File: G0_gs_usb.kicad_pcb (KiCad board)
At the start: 2 copper layers, 25.9 x 53.3 mm, 54 parts, among them J1 USB_C_Receptacle_USB2.0, J2 CAN1, J3 CAN2, J4 Conn_01x03_Pin, U1 STM32G0B1CBTx, U2 TJA1042T-3, U3 TJA1042T-3, U4 XC6206PxxxMR

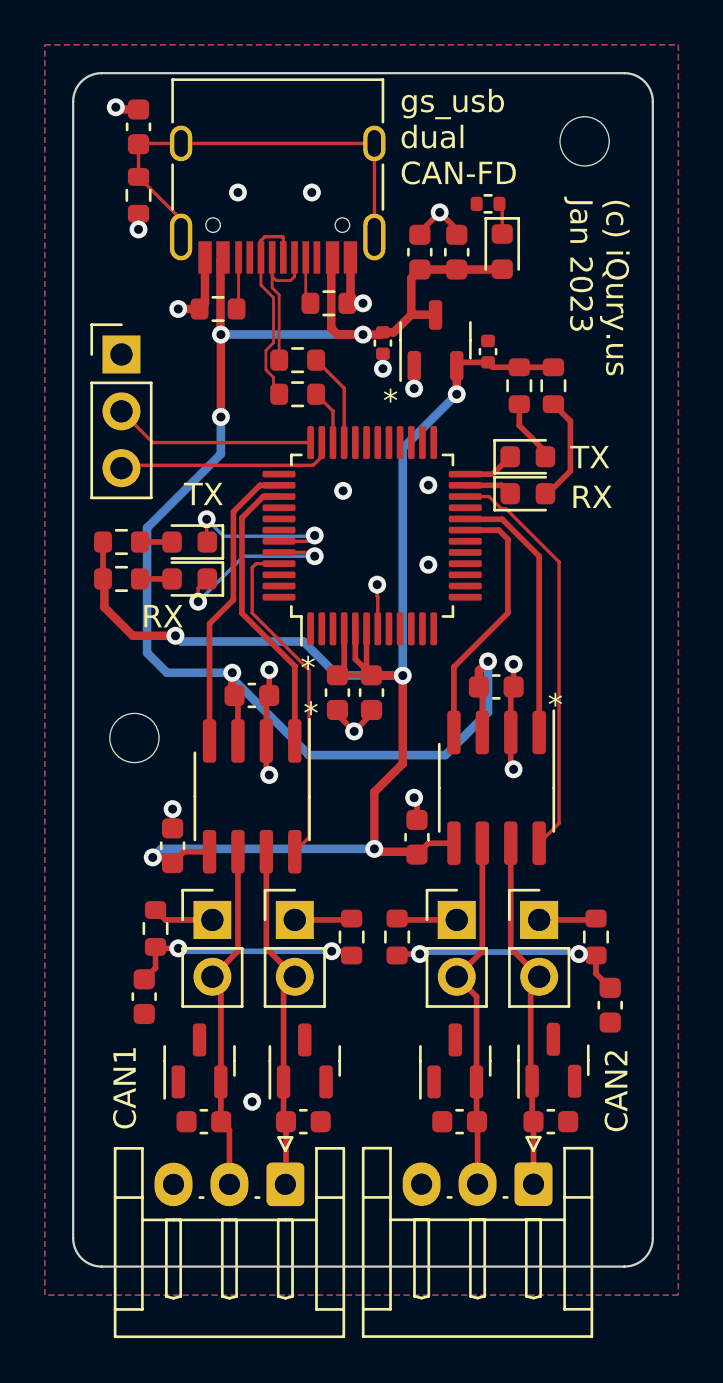
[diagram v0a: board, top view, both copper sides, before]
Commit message: Update footprints on R and C to 0402. Added 5V protection. Routed CAN RX/TX as diff pairs.
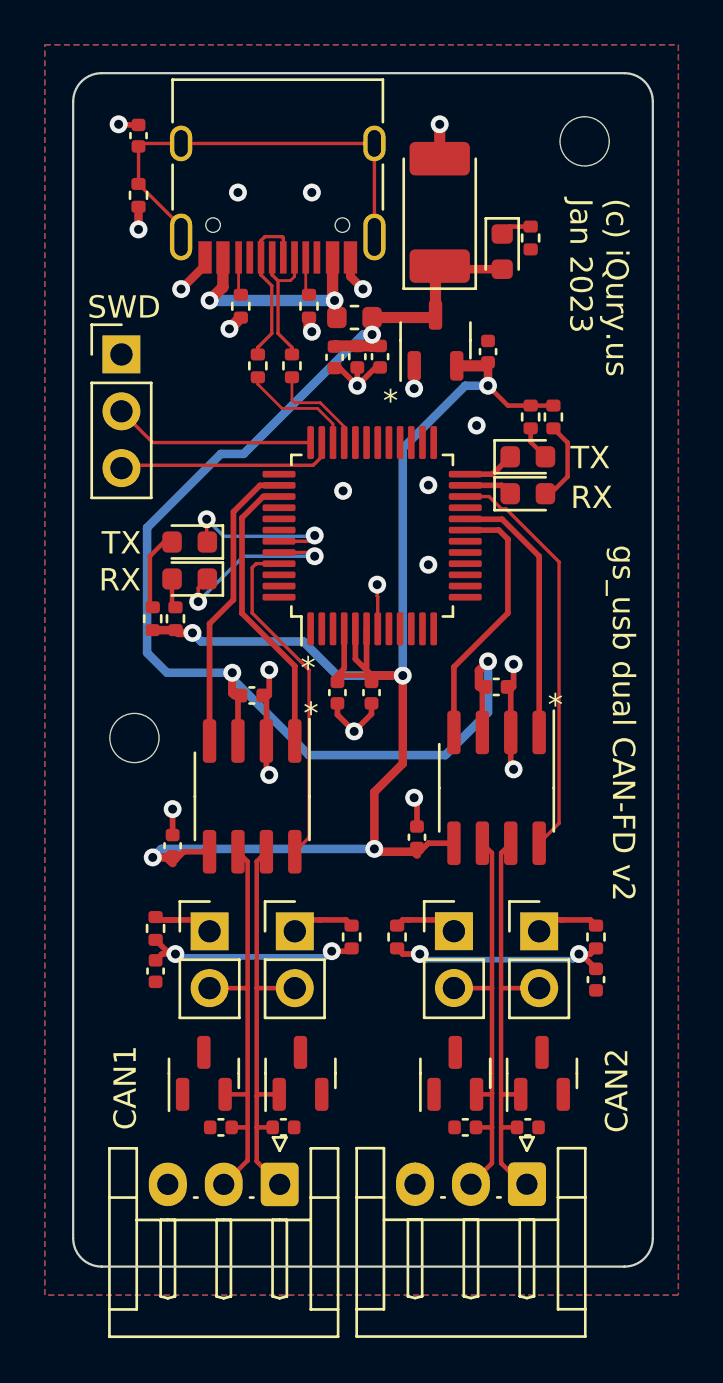
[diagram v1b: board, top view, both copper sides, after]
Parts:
- added D1: 5.3V, Diode_SMD:D_MELF, F.Cu at (68.5, 69.7)
- added F1: 500mA, Fuse:Fuse_0603_1608Metric, F.Cu at (64.6, 74.4)
- C1, C10, C11, C12, C13, C14, C15, C2, C3, C4, C5, C6, C7, C8, C9: footprint Capacitor_SMD:C_0603_1608Metric -> Capacitor_SMD:C_0402_1005Metric
- R1, R10, R11, R12, R13, R2, R3, R4, R5, R6, R7, R8, R9: footprint Resistor_SMD:R_0603_1608Metric -> Resistor_SMD:R_0402_1005Metric
- moved C13 6.45 mm to (64.8, 76.2), turned to 90 degrees
- moved C12 5.00 mm to (65.8, 76.2), turned to 90 degrees
- moved R11 3.70 mm to (55.6, 87.9), turned to 90 degrees
- moved R13 3.00 mm to (56.6, 87.9), turned to 90 degrees
- moved R14 2.44 mm to (72.5, 70.9), turned to -90 degrees
- moved C16 2.25 mm to (63.8, 76.2)
- moved R4 2.18 mm to (60.3, 76.6), turned to -90 degrees
- moved R12 1.48 mm to (72.5, 78.9)
- moved R10 1.40 mm to (73.5, 78.9)
- moved C7 1.31 mm to (75.4, 104.0)
- moved C2 1.25 mm to (55.8, 103.6)
- moved C8 1.06 mm to (72.4, 110.6)
- moved R2 1.02 mm to (59.6, 73.9), turned to 90 degrees
- moved C3 0.92 mm to (61.5, 110.6)
- moved R3 0.90 mm to (62.6, 73.9), turned to 90 degrees
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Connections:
- net /CAN1_H renamed /CAN1_P
- net /CAN1_L renamed /CAN1_N
- net /CAN2_H renamed /CAN2_P
- net /CAN2_L renamed /CAN2_N
- J1 pad A4: /5V -> Net-(F1-Pad2)
- J1 pad A9: /5V -> Net-(F1-Pad2)
- J1 pad B4: /5V -> Net-(F1-Pad2)
- J1 pad B9: /5V -> Net-(F1-Pad2)
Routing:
- net Net-(F1-Pad2): track 0.00 -> 10.5 mm, vias 0 -> 2
- net /5V: track 66.6 -> 57.5 mm, vias 5 -> 3
- net /3.3V: track 71.6 -> 67.7 mm
- net /CAN2_P: track 16.0 -> 19.3 mm
- net /CAN1_N: track 15.7 -> 18.9 mm
- net /CAN1_P: track 15.7 -> 18.9 mm
- net /CAN2_N: track 16.1 -> 19.2 mm
- net /USB_DP: track 2.47 -> 5.24 mm
- net Net-(D7-A): track 1.44 -> 3.59 mm
- net /D+: track 9.46 -> 7.52 mm
- net Net-(D8-A): track 2.83 -> 1.54 mm
- net Net-(D6-A): track 4.84 -> 3.73 mm
- net Net-(J1-CC2): track 2.34 -> 1.71 mm
- net GND: track 28.3 -> 28.6 mm, vias 21 -> 23
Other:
- board text added: "Not isolated"
- board text added: "SWD"
- board text added: "gs_usb dual CAN-FD v2"
- board text removed: "gs_usb dual CAN-FD"

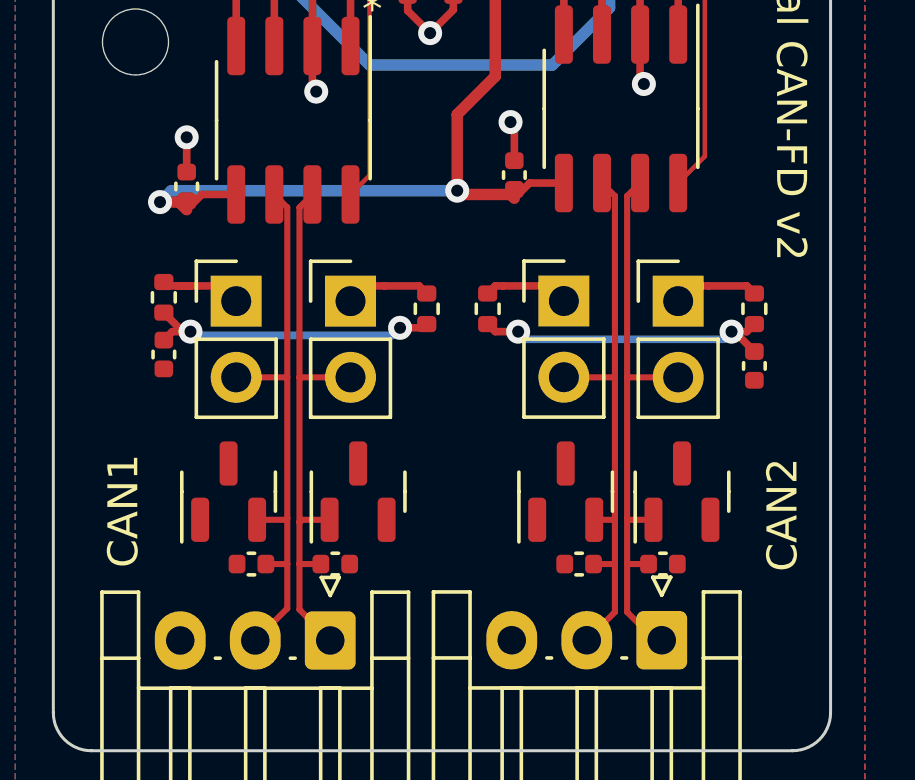
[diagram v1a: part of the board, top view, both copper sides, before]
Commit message: Use better TVS diodes.
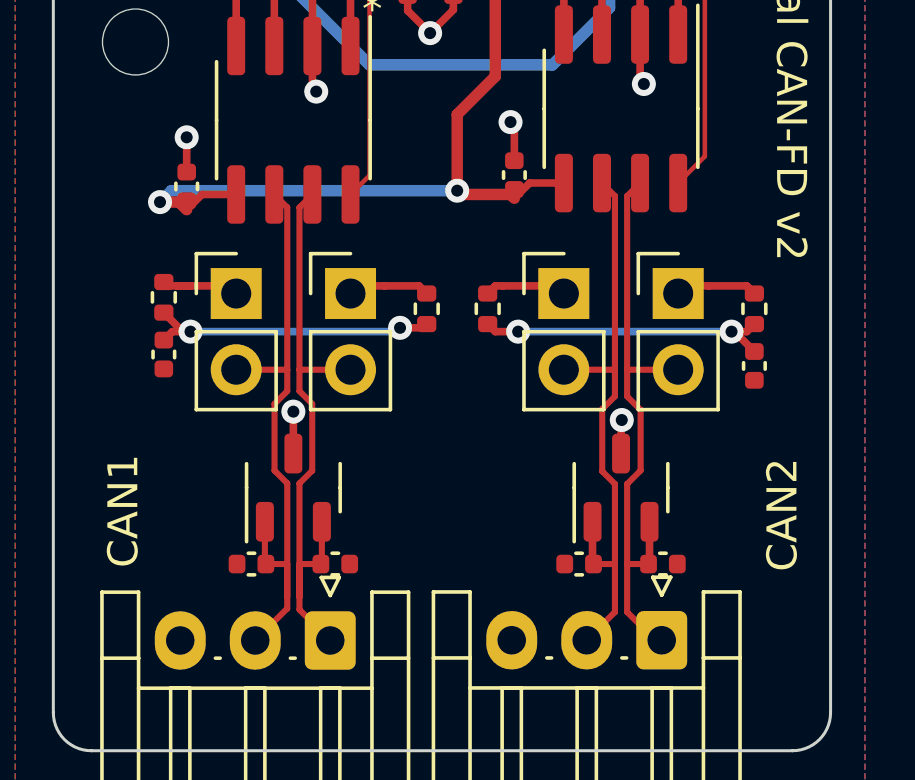
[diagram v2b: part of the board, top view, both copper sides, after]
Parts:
- removed the D4 at (62.2, 108.2)
- removed the D5 at (57.9, 108.2)
- D2, D3: value MMBZ27VC -> PSM712; footprint Package_TO_SOT_SMD:SOT-23 -> Package_TO_SOT_SMD:SOT-23-3
- moved D3 9.08 mm to (60.1, 108.1)
- moved D2 2.04 mm to (71.0, 108.1)
- moved JP1 0.25 mm to (72.9, 101.6)
- moved JP3 0.25 mm to (62.0, 101.6)
- moved JP4 0.25 mm to (58.2, 101.6)
- moved JP2 0.25 mm to (69.1, 101.6)
- renumbered D6 to D4, D7 to D5, D8 to D6, D9 to D7, D10 to D8
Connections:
- D2 pad 1: /CAN2_P -> /CAN2_N
- D2 pad 2: GND -> /CAN2_P
- D2 pad 3: unconnected-(D2-A-Pad3) -> GND
- D3 pad 1: GND -> /CAN1_N
- D3 pad 2: /CAN2_N -> /CAN1_P
- D3 pad 3: unconnected-(D3-A-Pad3) -> GND
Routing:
- net GND: track 28.6 -> 31.2 mm, vias 23 -> 25
- net /CAN1_N: track 18.9 -> 20.8 mm
- net /CAN1_P: track 18.9 -> 20.8 mm
- net /CAN2_N: track 19.2 -> 20.3 mm
- net /CAN2_P: track 19.3 -> 20.2 mm

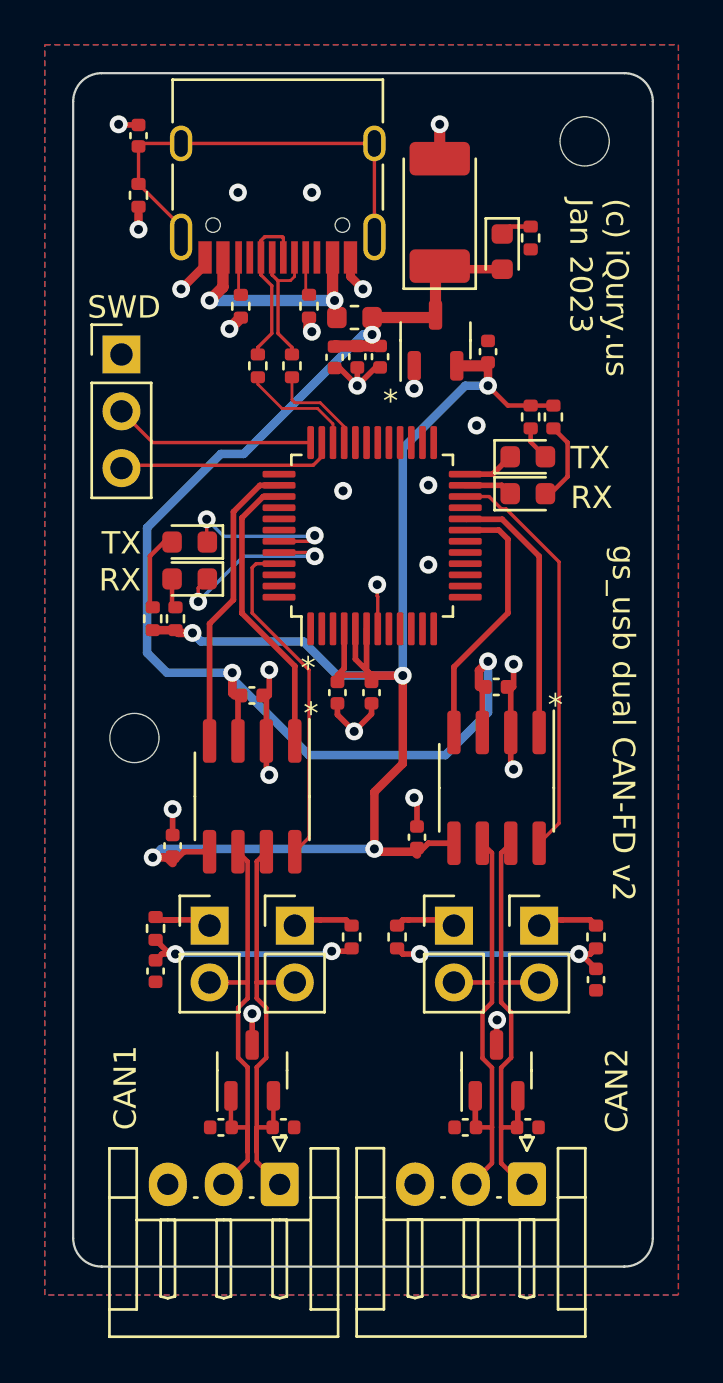
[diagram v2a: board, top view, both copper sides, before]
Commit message: Update TVS diodes. Add reset button.
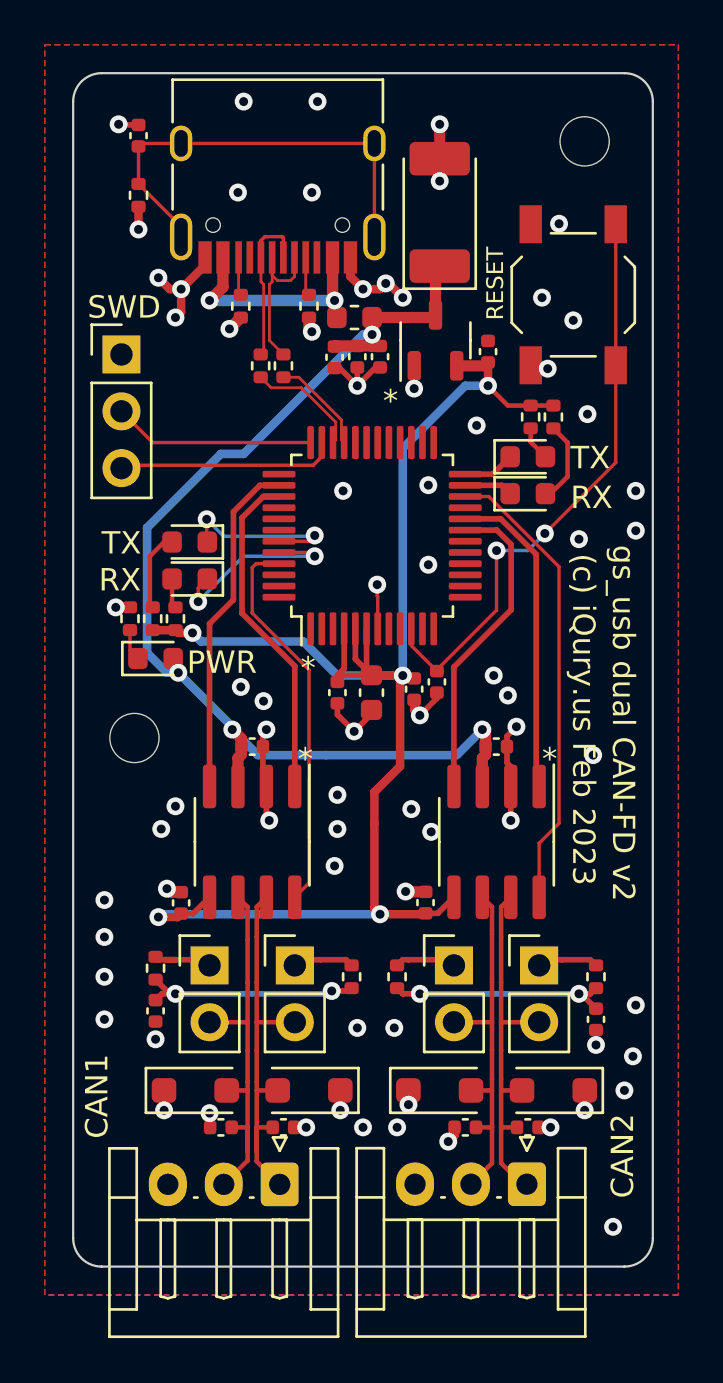
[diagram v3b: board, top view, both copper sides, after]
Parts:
- removed D2, D3: PSM712, Package_TO_SOT_SMD:SOT-23-3
- added C18: 100nF, Capacitor_SMD:C_0402_1005Metric, F.Cu at (67.3, 91.0)
- added C19: 100nF, Capacitor_SMD:C_0402_1005Metric, F.Cu at (68.3, 90.7)
- added D10: D_TVS, Diode_SMD:D_SOD-123F, F.Cu at (68.5, 109.0)
- added D11: D_TVS, Diode_SMD:D_SOD-123F, F.Cu at (62.6, 109.0)
- added D12: D_TVS, Diode_SMD:D_SOD-123F, F.Cu at (57.5, 109.0)
- added D9: D_TVS, Diode_SMD:D_SOD-123F, F.Cu at (73.5, 109.0)
- added SW1: SW_Push_Dual, Button_Switch_SMD:SW_SPST_TL3342, F.Cu at (74.4, 73.4)
- C14: value 10nF -> 10uF; footprint Capacitor_SMD:C_0402_1005Metric -> Capacitor_SMD:C_0603_1608Metric
- moved R14 24.7 mm to (54.6, 87.9), turned to 90 degrees
- moved D8 23.9 mm to (55.8, 89.7), turned to 0 degrees
- moved C10 2.95 mm to (67.8, 100.6)
- moved C5 2.67 mm to (71.0, 93.6)
- moved C11 2.58 mm to (56.9, 100.6)
- moved U3 2.41 mm to (71.0, 97.9)
- moved C6 2.29 mm to (60.1, 93.6)
- moved U2 2.03 mm to (60.1, 97.9)
- moved JP1 1.78 mm to (72.9, 103.4)
- moved JP2 1.78 mm to (69.1, 103.4)
- moved JP3 1.78 mm to (62.0, 103.4)
- moved JP4 1.78 mm to (58.2, 103.4)
- moved C2 1.78 mm to (55.8, 105.4)
- moved C7 1.78 mm to (75.4, 105.8)
- moved R6 1.78 mm to (75.4, 103.9)
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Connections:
- U1 pad 10: unconnected-(U1-PF2-Pad10) -> /~{RESET}
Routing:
- net /~{RESET}: track 0.00 -> 26.5 mm, vias 0 -> 2
- net GND: track 31.2 -> 40.0 mm, vias 25 -> 74
- net /5V: track 57.5 -> 51.3 mm, vias 3 -> 4
- net /CAN1_SBY: track 15.3 -> 19.9 mm
- net /CAN2_P: track 20.2 -> 17.0 mm
- net /CAN2_N: track 20.3 -> 17.0 mm
- net /CAN1_P: track 20.8 -> 17.9 mm
- net /CAN1_N: track 20.8 -> 17.9 mm
- net /CAN2_RX: track 11.7 -> 14.2 mm
- net /3.3V: track 67.7 -> 70.1 mm
- net /CAN2_TX: track 11.9 -> 14.3 mm
- net /CAN2_SBY: track 18.3 -> 20.6 mm
- net /CAN1_TX: track 13.0 -> 15.0 mm
- net /CAN1_RX: track 13.2 -> 15.2 mm
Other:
- board text added: "(c) iQury.us Feb 2023"
- board text added: "PWR"
- board text added: "RESET"
- board text removed: "(c) iQury.us Jan 2023"
